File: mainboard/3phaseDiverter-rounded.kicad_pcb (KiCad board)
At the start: 2 copper layers, 144.8 x 120.6 mm, 98 parts, among them CN9 SMA, IC1 ATmega328-P, IC2 LM358, J0 FTDI, J1 RESET, J10 D10, J11 D11, J12 D12, J13 D13, J14 +5V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

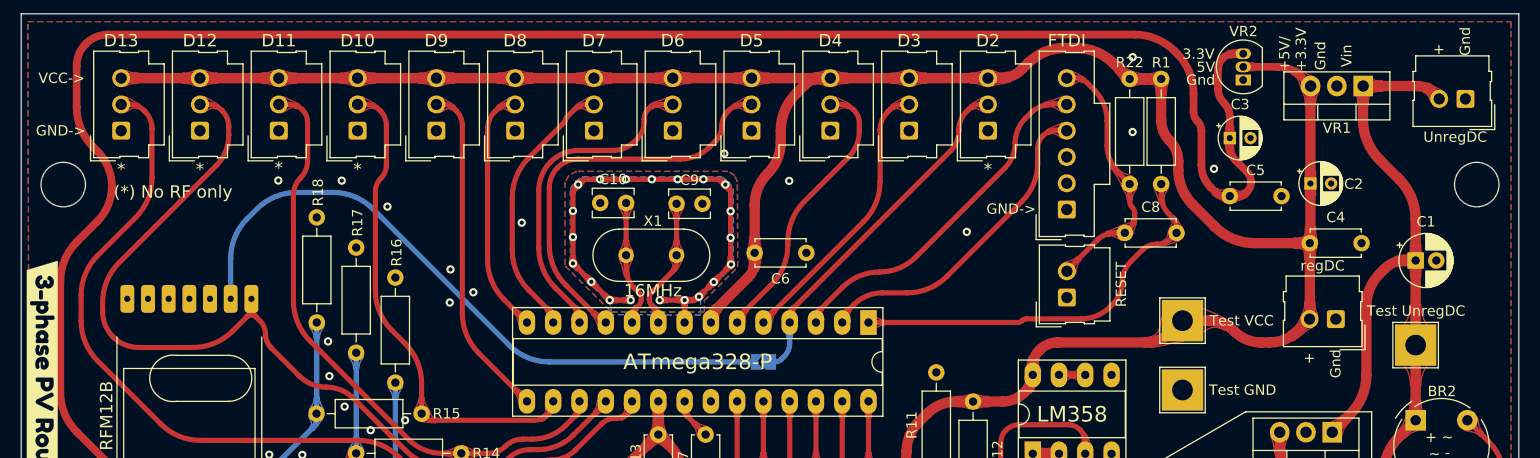
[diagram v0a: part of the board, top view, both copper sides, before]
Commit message: New PCB
New PCB with separated ground around crystal, inductance for AVCC, dual optional power supply, Molex SL connectors
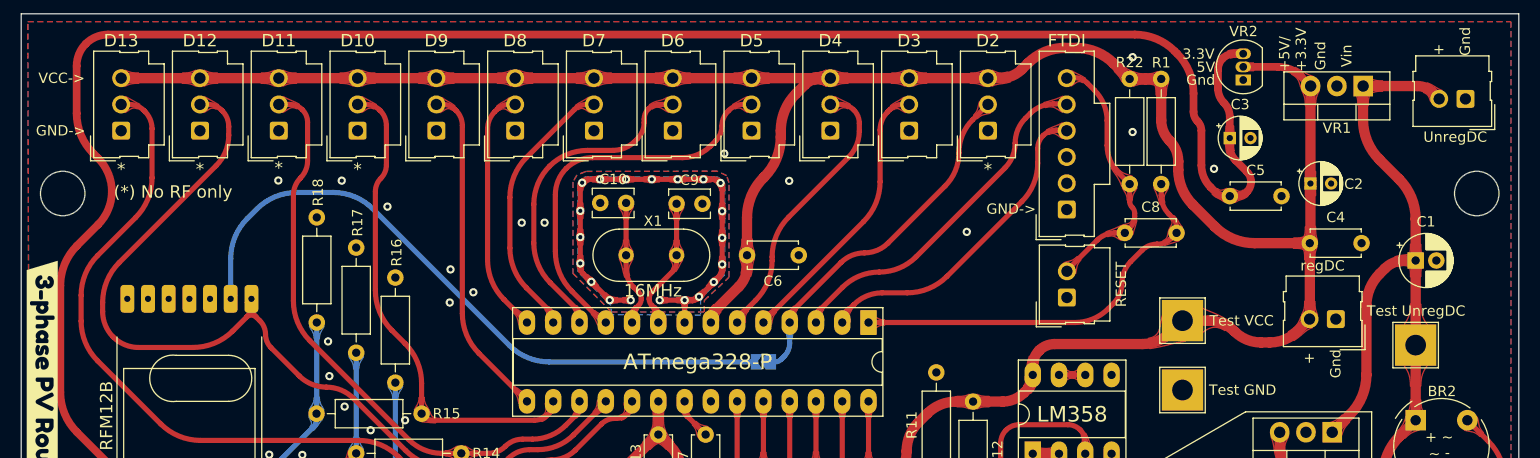
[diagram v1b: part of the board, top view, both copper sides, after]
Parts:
- moved REF** 0.87 mm to (19.3, 32.6)
- moved REF** 0.86 mm to (156.0, 32.6)
- moved C6 0.77 mm to (90.4, 38.6)
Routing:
- net GND: track 47.8 -> 46.2 mm, vias 81 -> 82
- net /D5: track 39.0 -> 37.9 mm
